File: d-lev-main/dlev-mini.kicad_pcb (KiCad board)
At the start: 2 copper layers, 128 x 61 mm, 9 parts, among them J1 20854-005E-02, J2 Tag-Connect TC2030-NL, J3 20854-005E-02, J4 USB_C_Receptacle_USB2.0, U1 AC608, U3 25LCxxx

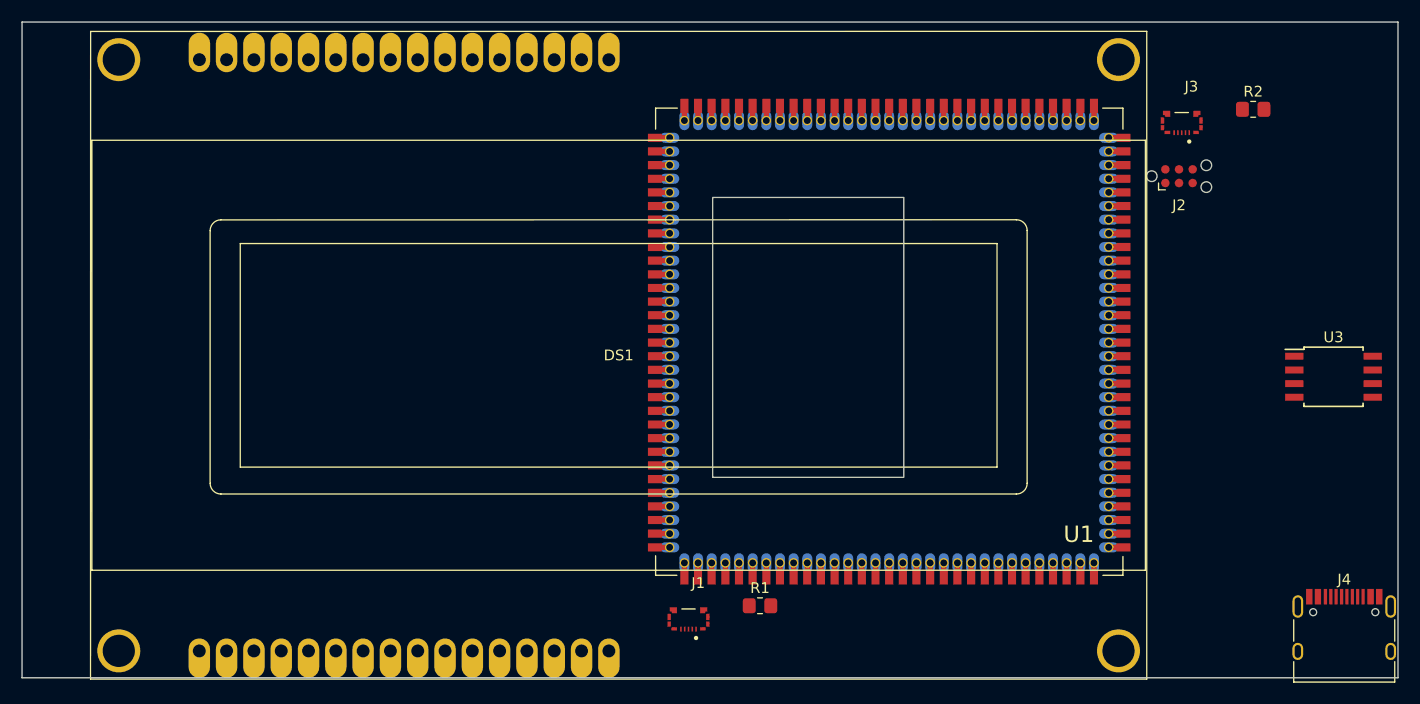
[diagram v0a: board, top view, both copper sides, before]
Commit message: Add block diagram
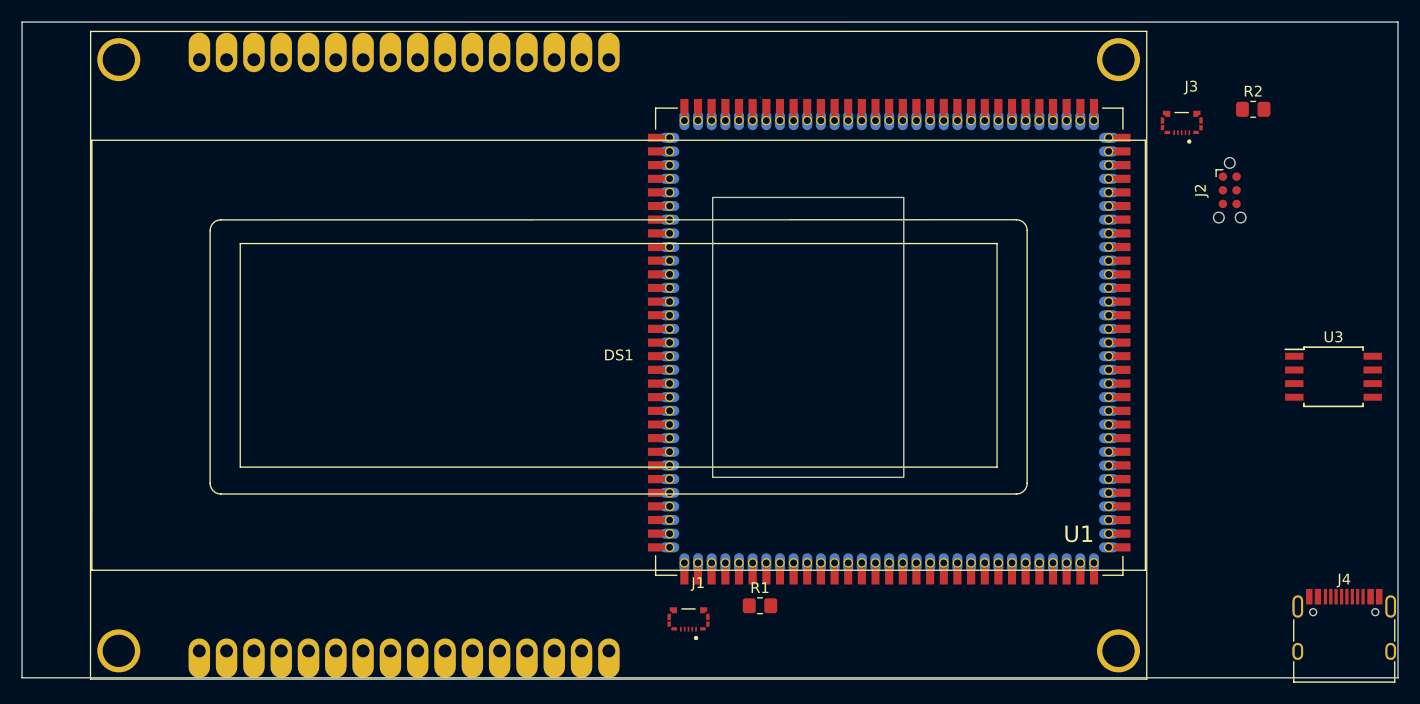
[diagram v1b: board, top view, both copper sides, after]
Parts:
- moved J2 4.90 mm to (186.8, 66.2), turned to -90 degrees

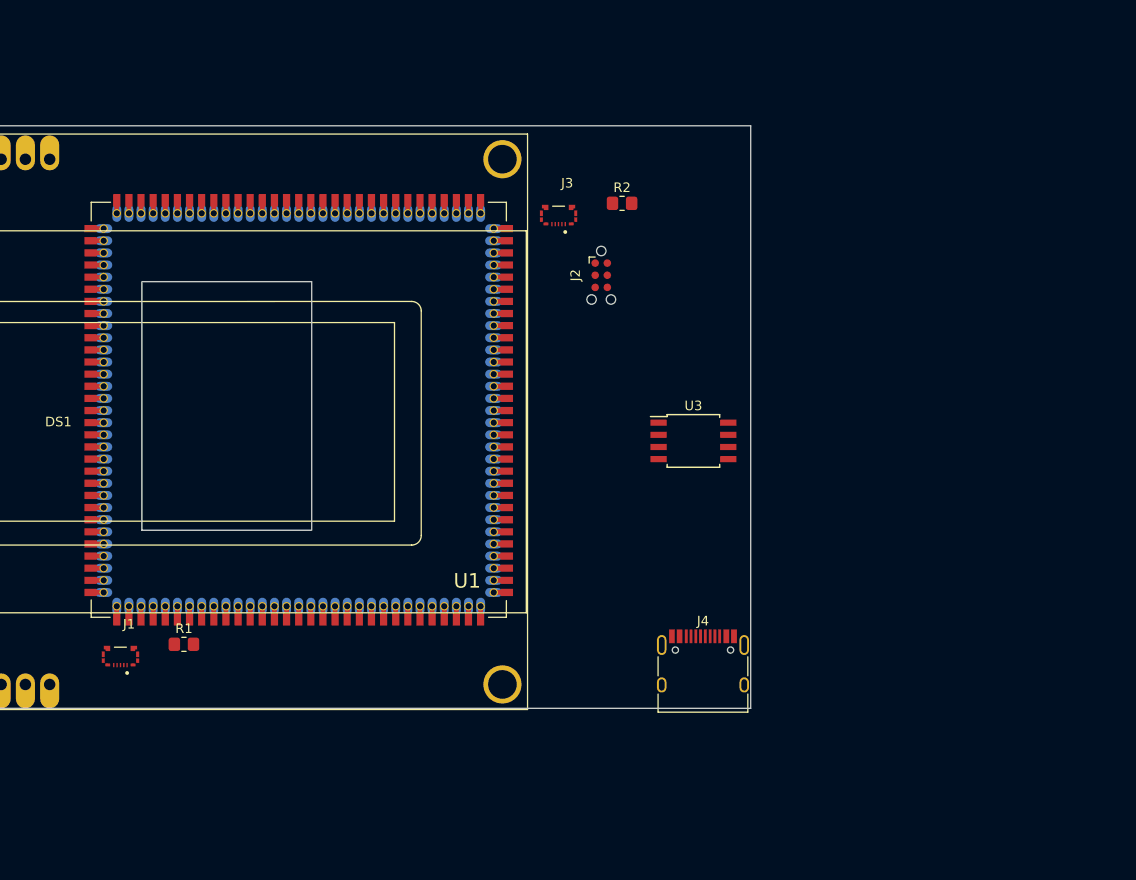
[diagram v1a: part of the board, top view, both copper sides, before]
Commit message: Many changes
Reorganized libraries to share between projects
Set up JLC 2- and 4- layer design rules
Finished copying over most of the schematic (excluding I/O board)
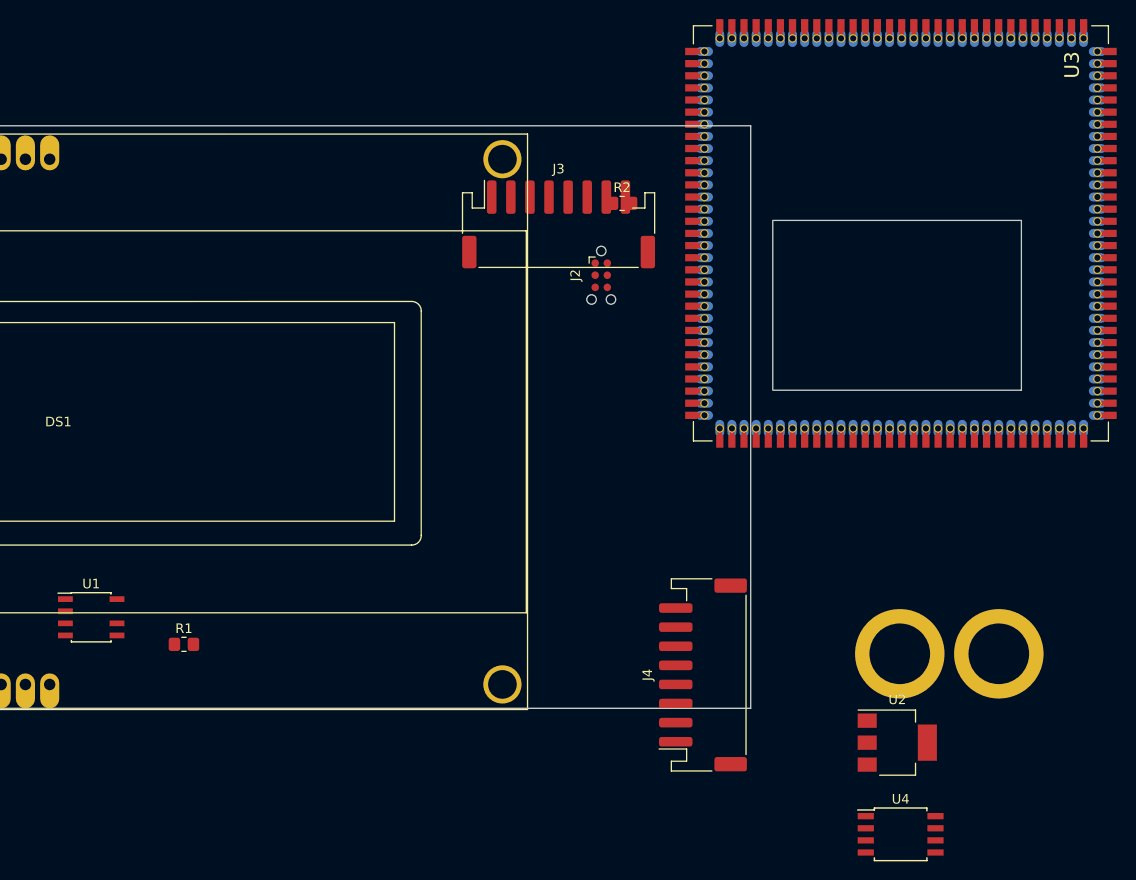
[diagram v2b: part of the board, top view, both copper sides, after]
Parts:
- removed J1: 20854-005E-02, footprints:I-PEX_20854-005E-02
- added H3: MountingHole, d-lev:SMTSO-M4, F.Cu at (218.1, 95.8)
- added H4: MountingHole, d-lev:SMTSO-M4, F.Cu at (228.5, 95.8)
- added U2: AMS1117-3.3, Package_TO_SOT_SMD:SOT-223-3_TabPin2, F.Cu at (217.8, 115.1)
- added U4: 25LCxxx, Package_SO:SOIC-8W_5.3x5.3mm_P1.27mm, F.Cu at (218.2, 124.7)
- DS1: footprint footprints:ERM2004-1 -> d-lev:ERM2004-1
- J3: value 20854-005E-02 -> S8B-PH-SM4-TB; footprint footprints:I-PEX_20854-005E-02 -> Connector_JST:JST_PH_S8B-PH-SM4-TB_1x08-1MP_P2.00mm_Horizontal
- J4: value USB_C_Receptacle_USB2.0 -> S8B-PH-SM4-TB; footprint Connector_USB:USB_C_Receptacle_HRO_TYPE-C-31-M-12 -> Connector_JST:JST_PH_S8B-PH-SM4-TB_1x08-1MP_P2.00mm_Horizontal
- U1: value AC608 -> TPS54331; footprint footprints:ac608 -> Package_SO:SOIC-8-N7_3.9x4.9mm_P1.27mm
- U3: value 25LCxxx -> AC608; footprint Package_SO:SOIC-8W_5.3x5.3mm_P1.27mm -> d-lev:ac608
- turned J4 to 90 degrees
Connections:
- net vol_sq_o renamed /pitch_quad_i
- J2 pad 2: /AC608/TMS -> /FPGA/TMS
- J2 pad 3: /AC608/TDI -> /FPGA/TDI
- J2 pad 4: /AC608/TCK -> /FPGA/TCK
- J2 pad 6: /AC608/TDO -> /FPGA/TDO
- J3 pad 2: vol_quad_i -> GND
- J3 pad 4: vol_zero_i -> GND
- J3 pad 5: GND -> /pitch_sq_o
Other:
- copper layers 2 -> 4
- rule pad_to_mask_clearance: 0 -> 0.05

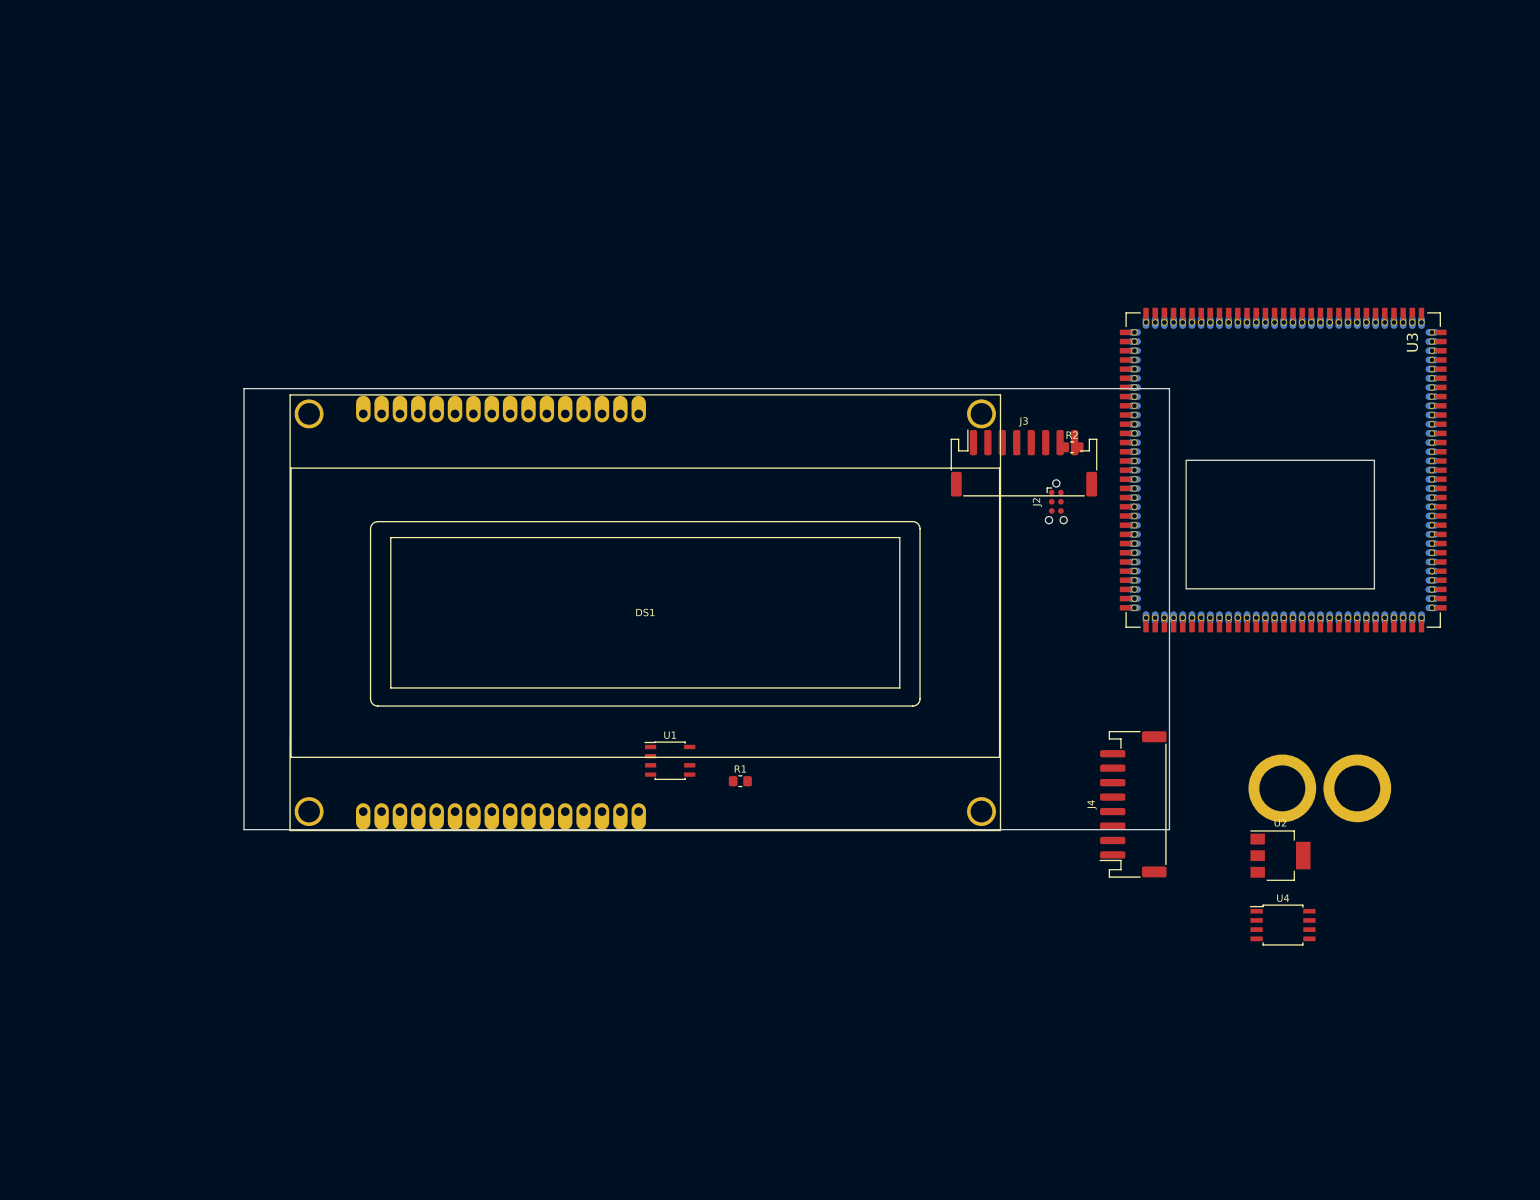
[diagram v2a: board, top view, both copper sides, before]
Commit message: clean up 3d models
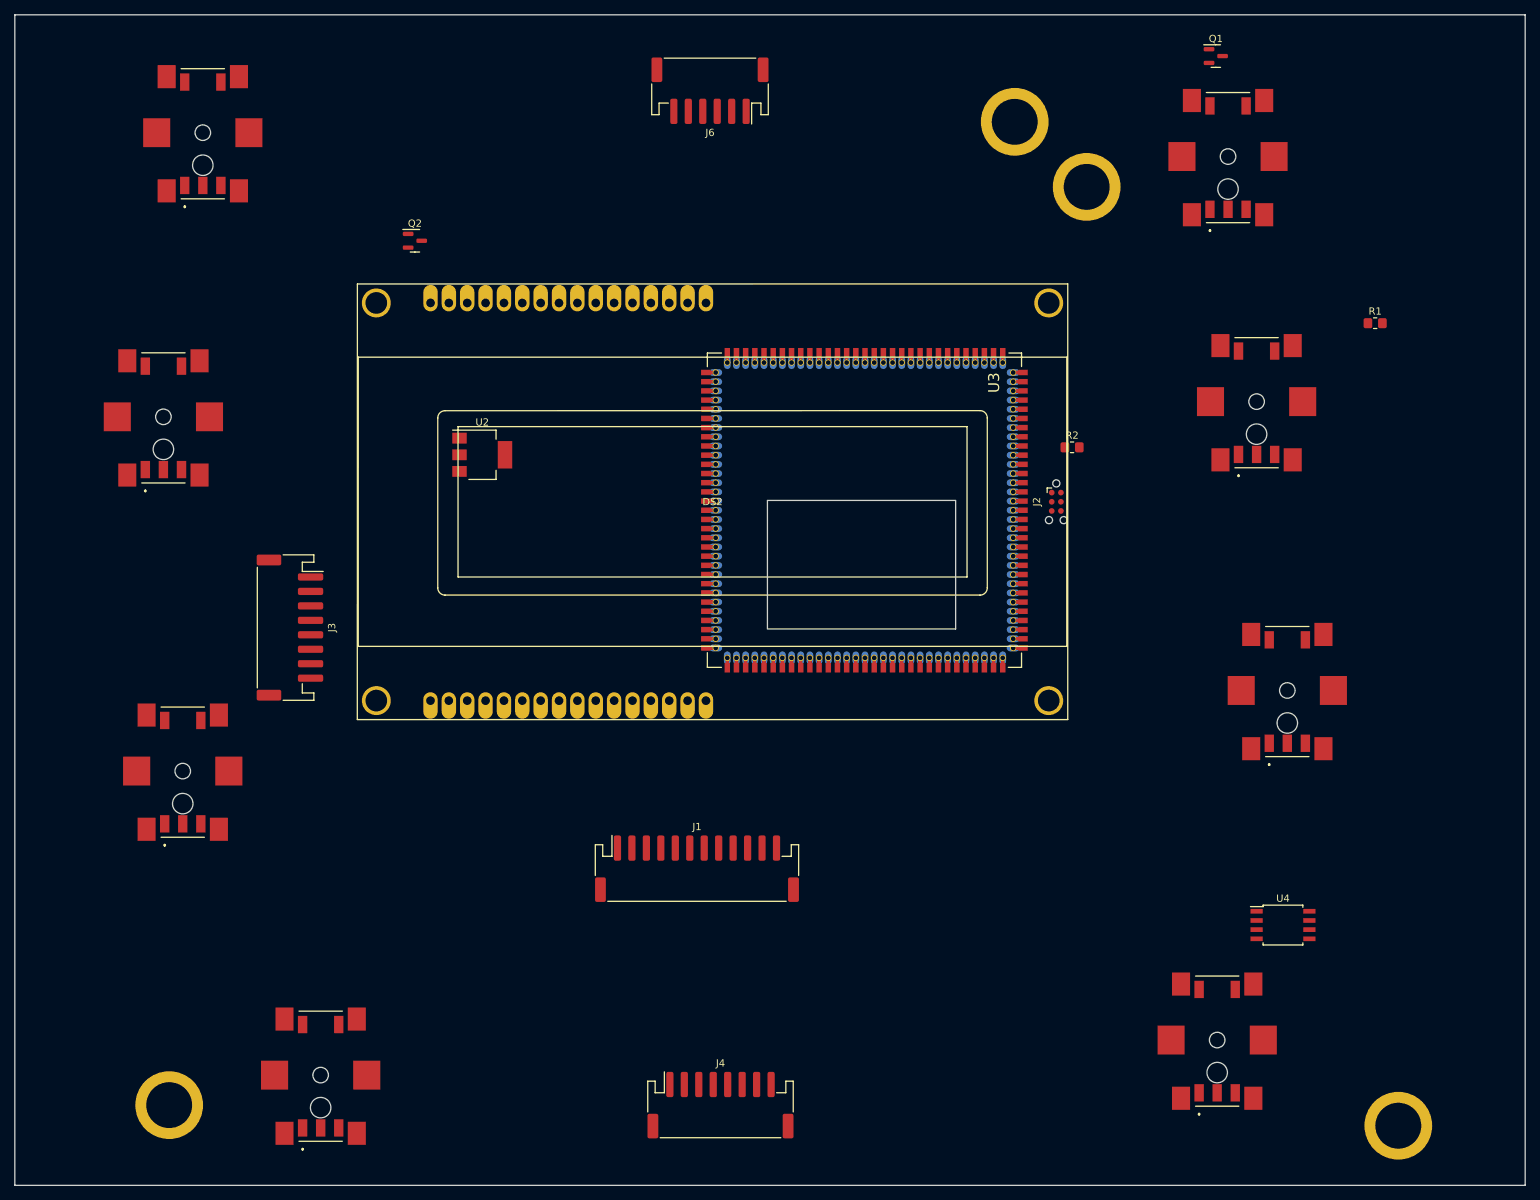
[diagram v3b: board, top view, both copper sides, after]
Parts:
- removed DS1: LCD-20X4B, d-lev:ERM2004-1
- removed U1: TPS54331, Package_SO:SOIC-8-N7_3.9x4.9mm_P1.27mm
- added DS2: LCD-20X4B, d-lev:ERM2004-1, F.Cu at (100.3, 38.6)
- added H1: MountingHole, d-lev:SMTSO-M4, F.Cu at (181.1, 3.60)
- added H2: MountingHole_Pad, d-lev:SMTSO-M4, F.Cu at (191.1, 12.6)
- added J1: IO_BOARD, d-lev:JST_PH_S12B-PH-SM4-TB_1x12-1MP_P2.00mm_Horizontal, F.Cu at (137.2, 116.9)
- added J6: S6B-PH-SM4-TB, d-lev:JST_PH_S6B-PH-SM4-TB_1x06-1MP_P2.00mm_Horizontal, F.Cu at (138.9, 9.30)
- added Q1: MMBT3904, Package_TO_SOT_SMD:SOT-23, F.Cu at (208.9, 4.50)
- added Q2: MMBT3904, Package_TO_SOT_SMD:SOT-23, F.Cu at (98.1, 30.1)
- added SW1: RotaryEncoder_Switch, d-lev:PEC11S9215FS0015, F.Cu at (68.8, 15.2)
- added SW2: RotaryEncoder_Switch, d-lev:PEC11S9215FS0015, F.Cu at (210.6, 18.6)
- added SW3: RotaryEncoder_Switch, d-lev:PEC11S9215FS0015, F.Cu at (214.6, 52.5)
- added SW4: RotaryEncoder_Switch, d-lev:PEC11S9215FS0015, F.Cu at (218.8, 92.4)
- added SW5: RotaryEncoder_Switch, d-lev:PEC11S9215FS0015, F.Cu at (209.1, 140.8)
- added SW6: RotaryEncoder_Switch, d-lev:PEC11S9215FS0015, F.Cu at (63.4, 54.5)
- added SW7: RotaryEncoder_Switch, d-lev:PEC11S9215FS0015, F.Cu at (66.0, 103.5)
- added SW8: RotaryEncoder_Switch, d-lev:PEC11S9215FS0015, F.Cu at (85.1, 145.6)
- J3, J4: footprint Connector_JST:JST_PH_S8B-PH-SM4-TB_1x08-1MP_P2.00mm_Horizontal -> d-lev:JST_PH_S8B-PH-SM4-TB_1x08-1MP_P2.00mm_Horizontal
- moved H4 170.1 mm to (64.2, 139.6)
- moved U2 123.5 mm to (107.5, 59.6)
- moved R1 108.3 mm to (230.9, 41.5)
- moved J3 104.0 mm to (80.8, 83.5), turned to -90 degrees
- moved J4 70.6 mm to (140.4, 149.6), turned to 0 degrees
- moved U3 58.2 mm to (138.6, 89.1)
- moved H3 49.3 mm to (234.2, 142.4)
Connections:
- net /pitch_quad_i renamed /FPGA/vol.quad
- net /pitch_sq_o renamed /FPGA/vol.sq
- net /pitch_zero_i renamed /FPGA/vol.zero
- net /vol_quad_i renamed /FPGA/pitch.quad
- net /vol_sq_o renamed /FPGA/pitch.sq
- net /vol_zero_i renamed /FPGA/pitch.zero
- U2 pad 1: unconnected-(U2-GND-Pad1) -> GND
- U2 pad 2: unconnected-(U2-VO-Pad2) -> +3V3
- U2 pad 3: unconnected-(U2-VI-Pad3) -> +5V
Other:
- board size 128 x 61 mm -> 208.9 x 161.9 mm
